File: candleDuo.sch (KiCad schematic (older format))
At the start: 76 parts

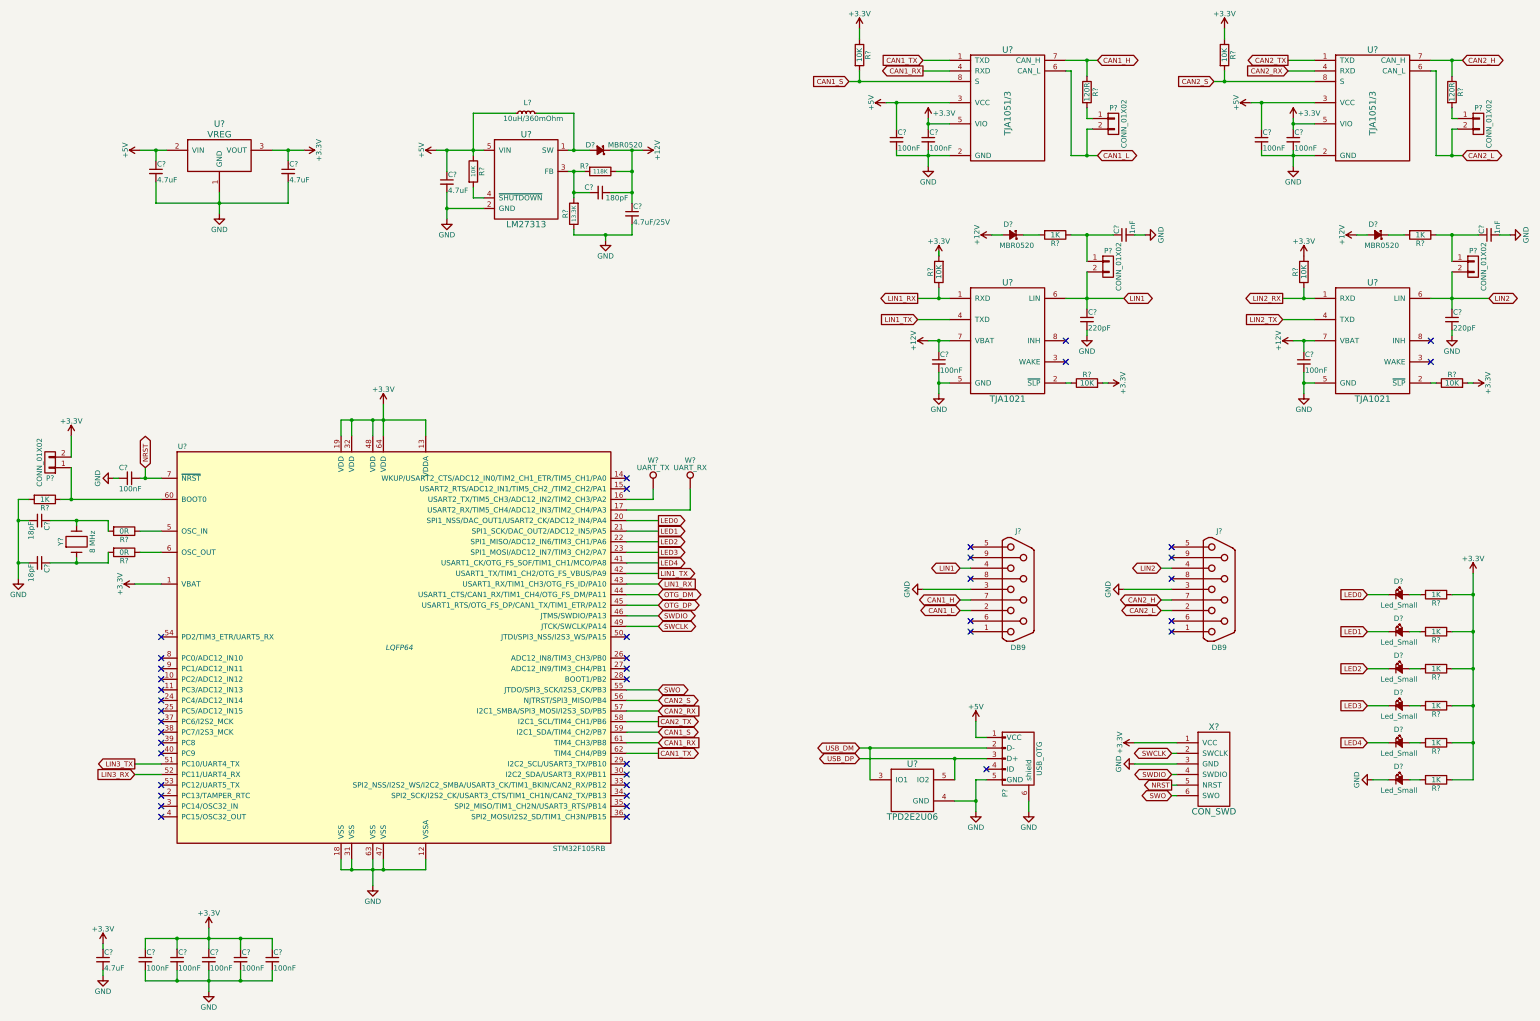
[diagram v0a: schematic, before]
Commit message: use duo leds
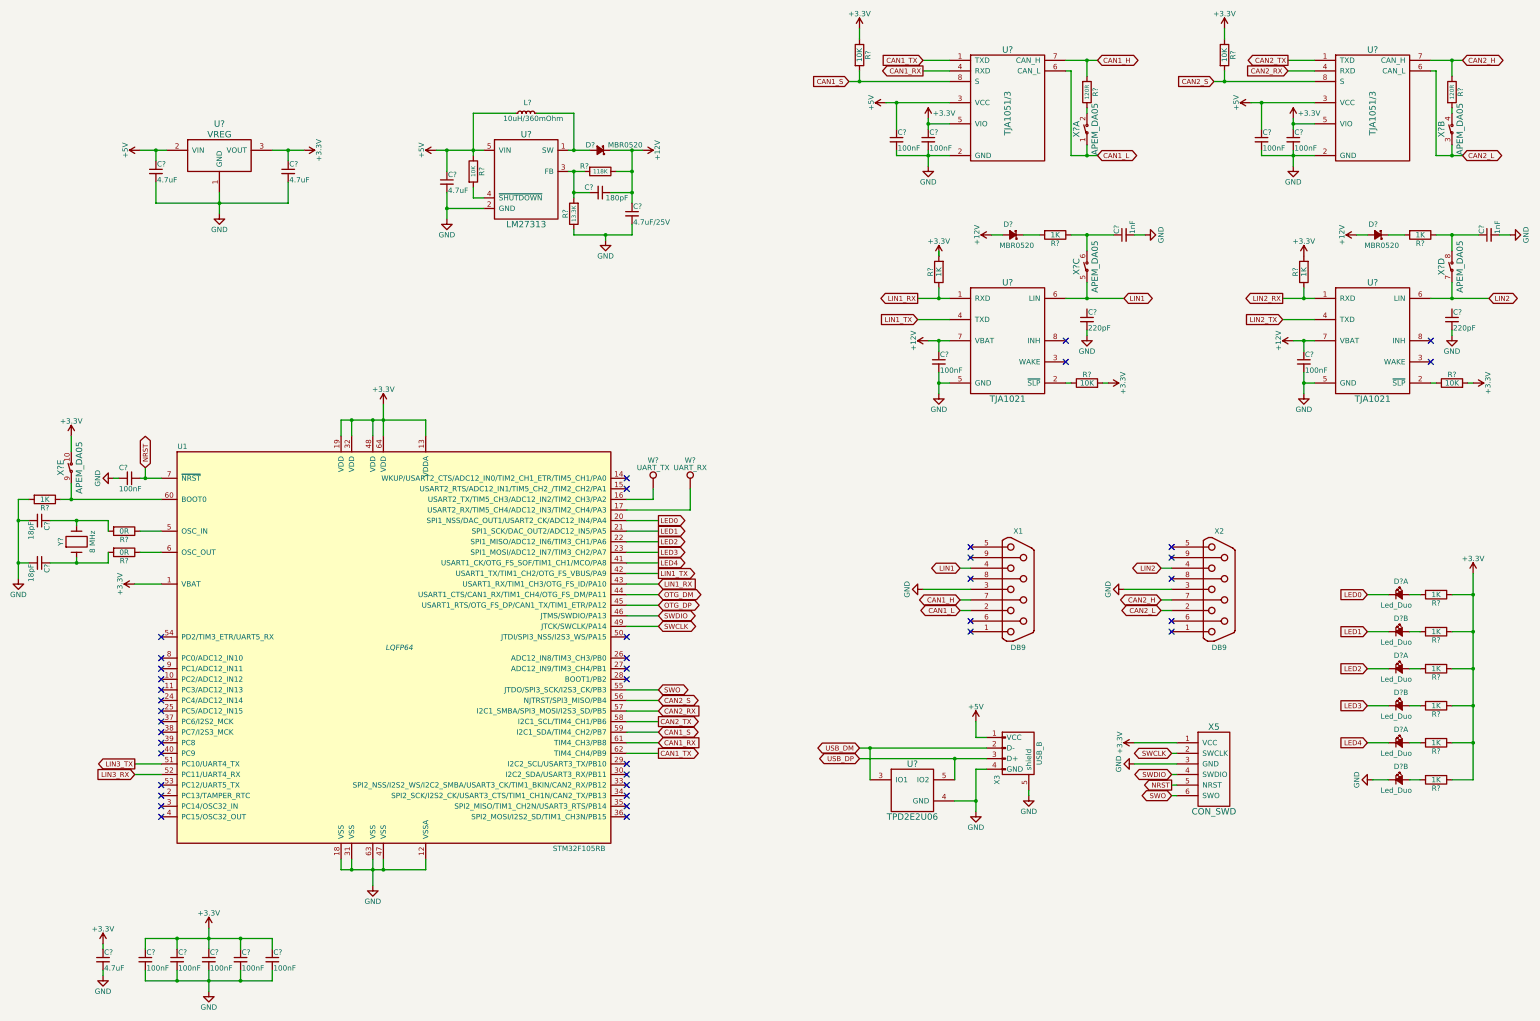
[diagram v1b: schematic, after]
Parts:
- removed D? (x6): Led_Small, symbol Led_Small
- removed P?: USB_OTG, symbol USB_OTG
- removed P? (x5): CONN_01X02, symbol CONN_01X02
- added D? (x6): Led_Duo, symbol Led_Duo
- added X3: USB_B, symbol USB_B
- added X? (x5): APEM_DA05, symbol APEM_DA05
- R? (x2): value 10K -> 1K
- gave numbers to parts that had none: 4
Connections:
- net +3V3: now also X?.10
- net +5V: now also X3.1 (VCC)
- net CAN1_H: now also R?.2; no longer R?.1
- net CAN1_L: now also X?.1
- net CAN2_L: now also X?.3
- net GND: now also D?.4 (K), X3.4 (GND), X3.5 (shield)
- net LED0: now also D?.2 (K)
- net LED1: now also D?.4 (K)
- net LED2: now also D?.2 (K)
- net LED3: now also D?.4 (K)
- net LED4: now also D?.2 (K)
- net LIN1: now also X?.5; no longer C?.1
- net LIN2: now also X?.7; no longer C?.1
- net USB_DM: now also X3.2 (D-)
- net USB_DP: now also X3.3 (D+)
- net at R?.1, U1.60 (BOOT0): now also X?.9
- net at R?.2: now also D?.1 (A) (x3)
- net at R?.2: now also D?.3 (A) (x3)
- net at R?.2: now also X?.4
- net at C?.1, R?.1: now also X?.6
- net at C?.1, R?.1: now also X?.8
- new net: R?.1, X?.2
- no-connect marks 42 -> 41

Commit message: assign most footprints
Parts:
- C1, C10, C15, C16, C17, C18, C19, C2, C20, C21, C22, C23, C24, C4, C5, C7, C8, C9: renamed from C?; footprint (none) -> Capacitors_SMD:C_0603
- C11, C12, C3, C6: renamed from C?; value 4.7uF -> 10uF; footprint (none) -> Capacitors_SMD:C_0805
- C13: renamed from C?; value 180pF -> 220pF; footprint (none) -> Capacitors_SMD:C_0603
- C14: renamed from C?; value 4.7uF/25V -> 10uF; footprint (none) -> Capacitors_SMD:C_0805
- D1, D2, D3: renamed from D?; footprint (none) -> Diodes_SMD:SOD-123
- R1, R10, R11, R12, R13, R14, R15, R16, R17, R18, R19, R2, R20, R21, R22, R3, R4, R5, R6, R7, R8, R9: renamed from R?; footprint (none) -> Resistors_SMD:R_0603
- U1: footprint LQFP64 -> Housings_QFP:LQFP-64_10x10mm_Pitch0.5mm
- U2: renamed from U?; value VREG -> MCP1754ST-3302E/MB; footprint (none) -> TO_SOT_Packages_SMD:SOT89-3_Housing
- U3: renamed from U?; footprint (none) -> TO_SOT_Packages_SMD:SOT-23-5
- U5, U6, U7, U8: renamed from U?; footprint (none) -> Housings_SOIC:SOIC-8_3.9x4.9mm_Pitch1.27mm
- W1, W2: renamed from W?; footprint (none) -> Measurement_Points:Measurement_Point_Round-SMD-Pad_Big
- X1, X2: footprint (none) -> Connect:DB9MC
- X3: footprint (none) -> Connect:USB_B
- X5: footprint (none) -> tagconnect:TC2030-NL
- gave numbers to parts that had none: 7
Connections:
- net +3V3: now also X4.2; no longer X4.10
- net CAN1_L: now also X4.3; no longer X4.1
- net CAN2_L: now also X4.7; no longer X4.3
- net LIN1: now also C18.1
- net LIN2: now also C23.1, X4.9; no longer X4.7
- net at R1.1, U1.60 (BOOT0): now also X4.1; no longer X4.9
- net at R10.1: now also X4.4; no longer X4.2
- net at R21.2: now also X4.8; no longer X4.4
- net at C24.1, R14.1: now also X4.10; no longer X4.8

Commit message: assign all footprints
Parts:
- D4, D5, D6: footprint (none) -> dialight:dialight-553-07xxx
- L1: footprint (none) -> SMD_Packages:SMD-1210_Pol
- U4: footprint (none) -> ti:DRL_R-PDSO-N5
- X4: footprint (none) -> apem:APEM_DA_05
- Y1: footprint (none) -> Crystals:ABM3

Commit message: some routing
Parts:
- removed U4: TPD2E2U06, ti:DRL_R-PDSO-N5, symbol TPD2E2U06
- added U4: onsemi-cm1231, TO_SOT_Packages_SMD:SOT-23-6, symbol onsemi-cm1231
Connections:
- net LIN3_RX is gone; now on net LIN2_RX: U1.52 (PC11/UART4_RX)
- net LIN3_TX is gone; now on net LIN2_TX: U1.51 (PC10/UART4_TX)
- net OTG_DM is gone; now on net USB_DM: U1.44 (USART1_CTS/CAN1_RX/TIM1_CH4/OTG_FS_DM/PA11)
- net OTG_DP is gone; now on net USB_DP: U1.45 (USART1_RTS/OTG_FS_DP/CAN1_TX/TIM1_ETR/PA12)
- net +5V: now also U4.5 (VP)
- net GND: now also U4.2 (VN)
- net USB_DM: now also U4.4 (Bin); no longer X3.2 (D-)
- net USB_DP: now also U4.3 (Ain); no longer X3.3 (D+)
- new net: U4.6 (Bout), X3.2 (D-)
- new net: U4.1 (Aout), X3.3 (D+)
